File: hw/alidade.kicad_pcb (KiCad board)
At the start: 2 copper layers, 277.2 x 107.5 mm, 194 parts, among them J1 TYPE-C-31-M-13C, M1 SK8701-01-005-SENSOR, SW1 SW_Push, SW10 SW_Push, SW11 SW_Push, SW12 SW_Push, SW13 SW_Push, SW14 SW_Push, SW15 SW_Push, SW16 SW_Push, SW17 SW_Push, SW18 SW_Push, SW19 SW_Push, SW2 SW_Push, SW20 SW_Push, SW21 SW_Push, SW3 SW_Push, SW4 SW_Push, SW5 SW_Push, SW6 SW_Push, SW7 SW_Push, SW8 SW_Push, SW9 SW_Push, U1 NPM1300-QEAA-R, U2 NRF54L15-QFAA-R, U3 ADS122S14IRTER, Y1 ABS07-32.768KHZ-T, Y2 ABM8G-32.000MHZ-B4Y-T

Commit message: Place ftdi parts
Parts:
- added C24: 47p, Alidade:C_0603_1608Metric, F.Cu at (199.6, 149.9)
- added C25: 47p, Alidade:C_0603_1608Metric, F.Cu at (191.8, 142.1)
- added C26: 100n, Alidade:C_0603_1608Metric, F.Cu at (198.1, 149.9)
- added C27: 4.7u, Alidade:C_0603_1608Metric, F.Cu at (193.0, 145.9)
- added C28: 100n, Alidade:C_0603_1608Metric, F.Cu at (193.0, 144.4)
- added R1: 27, Alidade:R_0603_1608Metric, F.Cu at (193.3, 142.1)
- added R26: 27, Alidade:R_0603_1608Metric, F.Cu at (199.5, 144.3)
- added U5: FT200XD, Alidade:DFN-10_FTD, F.Cu at (196.7, 146.1)
- added U6: USBLC6-2SC6, Alidade:SOT23-6L_STM, F.Cu at (196.7, 142.3)
- added rC24: 47p, Alidade:C_0603_1608Metric, F.Cu at (218.6, 143.1)
- added rC25: 47p, Alidade:C_0603_1608Metric, F.Cu at (211.1, 140.8)
- added rC26: 100n, Alidade:C_0603_1608Metric, F.Cu at (218.8, 146.6)
- added rC27: 4.7u, Alidade:C_0603_1608Metric, F.Cu at (211.1, 149.8)
- added rC28: 100n, Alidade:C_0603_1608Metric, F.Cu at (212.6, 149.8)
- added rR1: 27, Alidade:R_0603_1608Metric, F.Cu at (211.1, 144.1)
- added rR26: 27, Alidade:R_0603_1608Metric, F.Cu at (217.1, 143.1)
- added rU5: FT200XD, Alidade:DFN-10_FTD, F.Cu at (213.9, 146.1)
- added rU6: USBLC6-2SC6, Alidade:SOT23-6L_STM, F.Cu at (213.9, 142.4)
- L1, L2, rL1, rL2: value 2.2uH -> 2.2u
- turned C1 to 180 degrees
- turned rC1 to 180 degrees
- renumbered rU4 to rU2
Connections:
- C1 pad 1: Net-(U1C-VBUS) -> GND
- C1 pad 2: GND -> /PMIC/VBUS
- J1 pad A4: Net-(U1C-VBUS) -> /PMIC/VBUS
- J1 pad A6: unconnected-(J1-D+-PadA6) -> Net-(J1-D+-PadA6)
- J1 pad A7: unconnected-(J1-D--PadA7) -> Net-(J1-D--PadA7)
- J1 pad A9: Net-(U1C-VBUS) -> /PMIC/VBUS
- J1 pad B4: Net-(U1C-VBUS) -> /PMIC/VBUS
- J1 pad B6: unconnected-(J1-D+-PadB6) -> Net-(J1-D+-PadA6)
- J1 pad B7: unconnected-(J1-D--PadB7) -> Net-(J1-D--PadA7)
- J1 pad B9: Net-(U1C-VBUS) -> /PMIC/VBUS
- U1 pad 10: /MCU/PMICGPIO3 -> unconnected-(U1B-GPIO3-Pad10)
- U1 pad 21: Net-(U1C-VBUS) -> /PMIC/VBUS
- U1 pad 7: unconnected-(U1B-GPIO0-Pad7) -> /MCU/PMICINT
- U1 pad 8: /MCU/PMICINT -> /MCU/PMICGPIO1
- U1 pad 9: /MCU/PMICGPIO2 -> unconnected-(U1B-GPIO2-Pad9)
- U2 pad 23: /MCU/PMICGPIO2 -> /MCU/PMICINT
- U2 pad 24: /MCU/PMICGPIO3 -> /MCU/PMICGPIO1
- U2 pad 27: /MCU/PMICINT -> Net-(U2D-P0.02)
- U2 pad 3: unconnected-(U2B-P1.02/NFC1-Pad3) -> /MCU/CBUS0
- rC1 pad 1: Net-(rU1C-VBUS) -> rGND
- rC1 pad 2: rGND -> /PMIC/rVBUS
- rJ1 pad A4: Net-(rU1C-VBUS) -> /PMIC/rVBUS
- rJ1 pad A6: unconnected-(rJ1-D+-PadA6) -> Net-(rJ1-D+-PadA6)
- rJ1 pad A7: unconnected-(rJ1-D--PadA7) -> Net-(rJ1-D--PadA7)
- rJ1 pad A9: Net-(rU1C-VBUS) -> /PMIC/rVBUS
- rJ1 pad B4: Net-(rU1C-VBUS) -> /PMIC/rVBUS
- rJ1 pad B6: unconnected-(rJ1-D+-PadB6) -> Net-(rJ1-D+-PadA6)
- rJ1 pad B7: unconnected-(rJ1-D--PadB7) -> Net-(rJ1-D--PadA7)
- rJ1 pad B9: Net-(rU1C-VBUS) -> /PMIC/rVBUS
- rU1 pad 10: /MCU/rPMICGPIO3 -> unconnected-(rU1B-GPIO3-Pad10)
- rU1 pad 21: Net-(rU1C-VBUS) -> /PMIC/rVBUS
- rU1 pad 7: unconnected-(rU1B-GPIO0-Pad7) -> /MCU/rPMICINT
- rU1 pad 8: /MCU/rPMICINT -> /MCU/rPMICGPIO1
- rU1 pad 9: /MCU/rPMICGPIO2 -> unconnected-(rU1B-GPIO2-Pad9)
- rU2 pad 23: /MCU/rPMICGPIO2 -> /MCU/rPMICINT
- rU2 pad 24: /MCU/rPMICGPIO3 -> /MCU/rPMICGPIO1
- rU2 pad 27: /MCU/rPMICINT -> Net-(rU2D-P0.02)
- rU2 pad 3: unconnected-(rU4B-P1.02/NFC1-Pad3) -> /MCU/rCBUS0
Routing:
- net /PMIC/VBUS: track 0.00 -> 39.6 mm, vias 0 -> 3
- net /PMIC/rVBUS: track 0.00 -> 31.4 mm, vias 0 -> 2
- net Net-(U1C-VBUS): track 22.2 -> 0.00 mm, vias 2 -> 0
- net Net-(rU1C-VBUS): track 22.1 -> 0.00 mm, vias 2 -> 0
- net /MCU/SDA: track 0.00 -> 21.2 mm
- net /MCU/SCL: track 0.00 -> 17.9 mm
- net Net-(J1-D--PadA7): track 0.00 -> 8.67 mm, vias 0 -> 1
- net Net-(rJ1-D+-PadA6): track 0.00 -> 8.21 mm, vias 0 -> 2
- net Net-(rJ1-D--PadA7): track 0.00 -> 7.18 mm, vias 0 -> 1
- net Net-(J1-D+-PadA6): track 0.00 -> 6.85 mm, vias 0 -> 3
- net Net-(rR26-Pad1): track 0.00 -> 5.61 mm
- net Net-(rU5A-USBDM): track 0.00 -> 5.47 mm
- net Net-(U5A-USBDP): track 0.00 -> 5.26 mm
- net Net-(R1-Pad1): track 0.00 -> 5.12 mm
- net Net-(U5A-USBDM): track 0.00 -> 4.78 mm
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
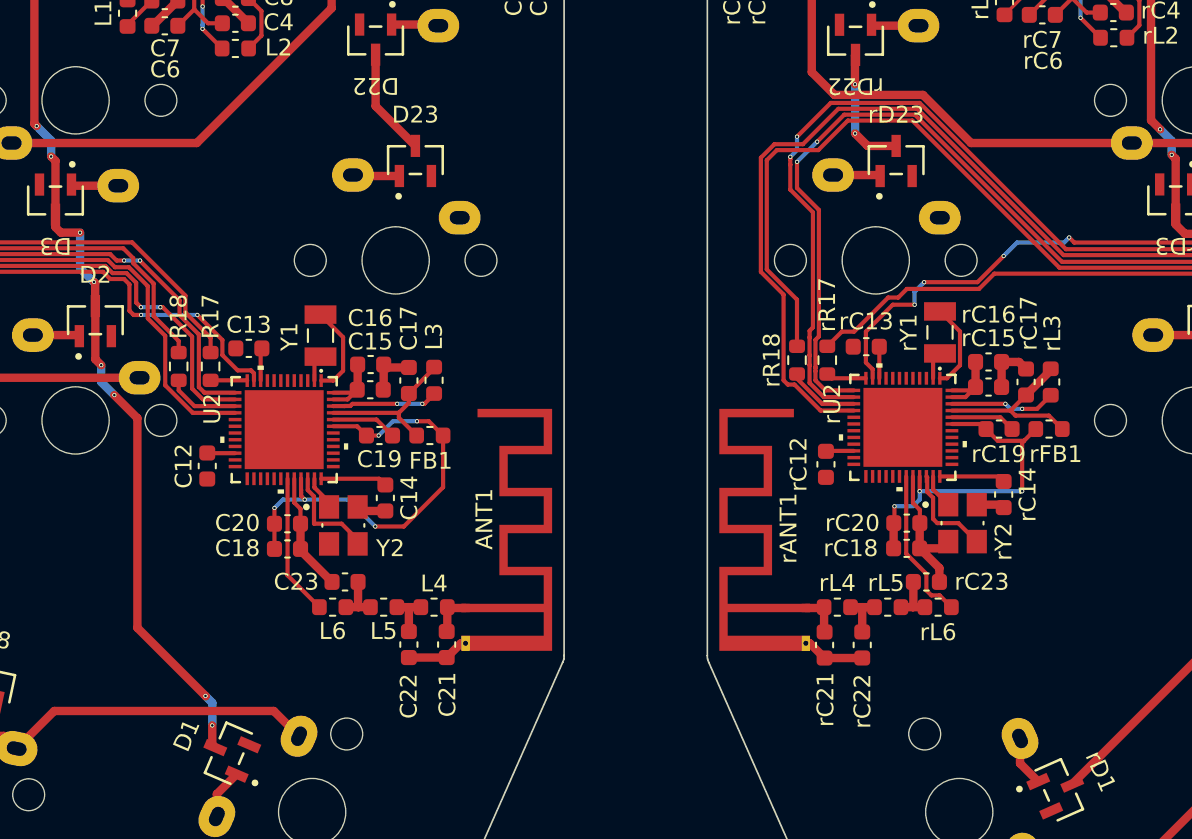
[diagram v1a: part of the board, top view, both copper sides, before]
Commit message: Remove mcu because it was wrong
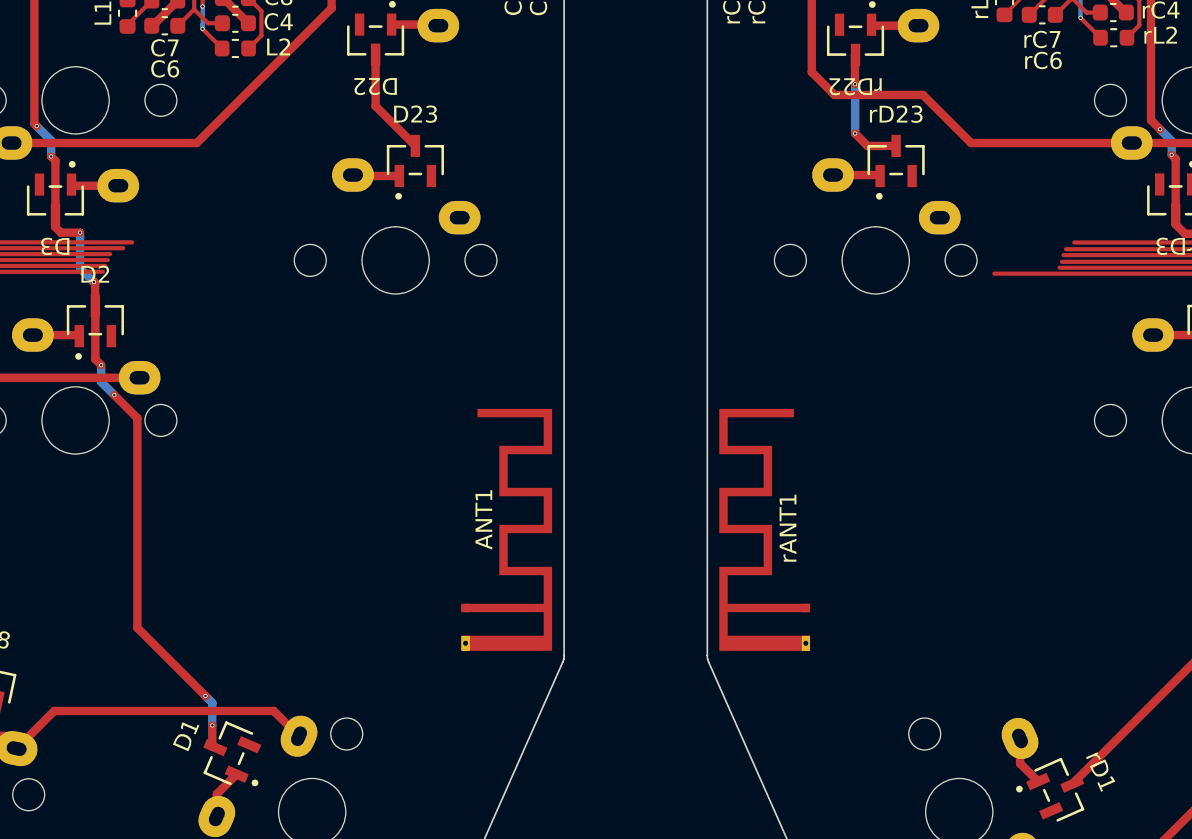
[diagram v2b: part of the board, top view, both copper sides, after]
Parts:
- removed C12, C13, C14, C15, rC12, rC13, rC14, rC15: 100n, Alidade:C_0603_1608Metric
- removed C16, rC16: 10u, Alidade:C_0603_1608Metric
- removed C17, C18, rC17, rC18: 2.2u, Alidade:C_0603_1608Metric
- removed C19, rC19: 10n, Alidade:C_0603_1608Metric
- removed C20, rC20: 2.2n, Alidade:C_0603_1608Metric
- removed C21, rC21: 0.3p, Alidade:C_0603_1608Metric
- removed C22, rC22: 2p, Alidade:C_0603_1608Metric
- removed C23, rC23: 1.5p, Alidade:C_0603_1608Metric
- removed FB1, rFB1: FB, Alidade:L_0603_1608Metric
- removed L3, rL3: 4.7u, Alidade:L_0603_1608Metric
- removed L4, L5, rL4, rL5: 3.5n, Alidade:L_0603_1608Metric
- removed L6, rL6: 2.7n, Alidade:L_0603_1608Metric
- removed R17, R18, rR17, rR18: 0, Alidade:R_0603_1608Metric
- removed U2, rU2: NRF54L15-QFAA-R, Alidade:QFN48_6X6
- removed Y1, rY1: ABS07-32.768KHZ-T, Alidade:XTAL_ABS07-32.768KHZ-1-T
- removed Y2, rY2: ABM8G-32.000MHZ-B4Y-T, Alidade:XTAL_ABM8G-32.000MHZ-B4Y-T
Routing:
- net /HID/rADCCS: track 92.9 -> 51.4 mm
- net /HID/rDRDY: track 89.0 -> 50.1 mm, vias 2 -> 0
- net /HID/rMISO: track 89.6 -> 52.9 mm, vias 2 -> 0
- net /HID/rMOSI: track 88.1 -> 54.3 mm
- net Net-(U2F-DECA): track 26.5 -> 0.00 mm, vias 5 -> 0
- net GND: track 54.8 -> 33.2 mm
- net rGND: track 53.5 -> 32.5 mm
- net Net-(rU2F-DECA): track 20.3 -> 0.00 mm, vias 3 -> 0
- net /HID/rFAULT: track 67.3 -> 49.1 mm, vias 4 -> 0
- net /HID/ADCCS: track 61.3 -> 47.1 mm
- net /HID/DRDY: track 62.4 -> 48.8 mm, vias 2 -> 0
- net /HID/FAULT: track 64.2 -> 50.9 mm, vias 2 -> 0
- net /HID/MISO: track 59.2 -> 46.0 mm, vias 2 -> 0
- net DVDD: track 22.5 -> 10.2 mm
- net rDVDD: track 21.4 -> 9.32 mm
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
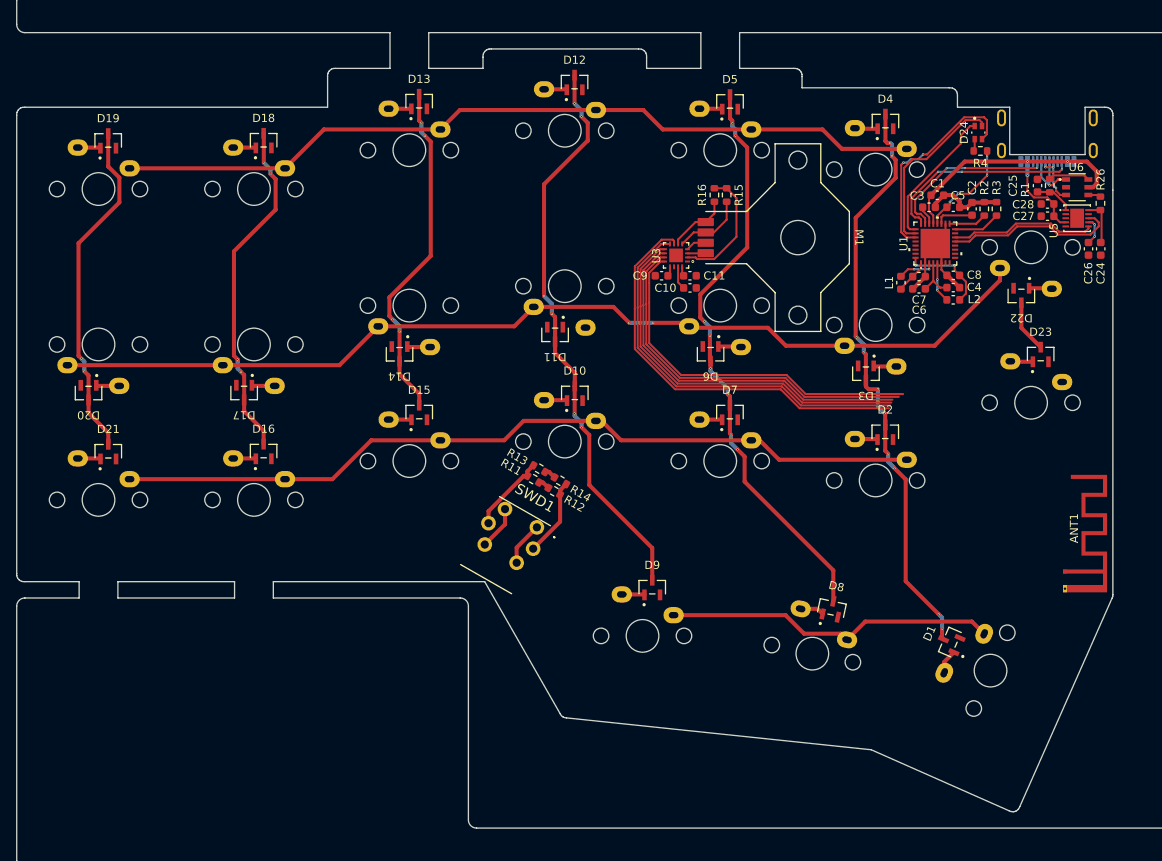
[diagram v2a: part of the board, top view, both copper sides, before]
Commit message: Add ground fills and attach left side
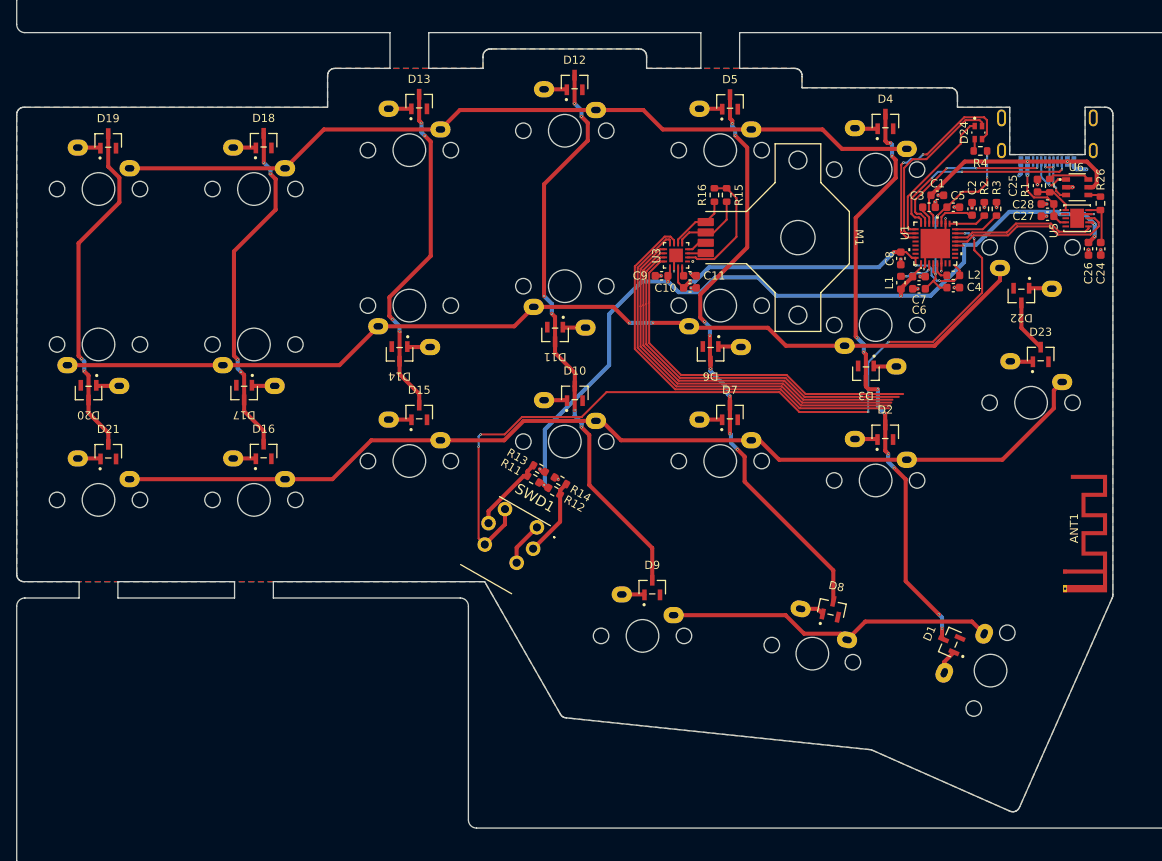
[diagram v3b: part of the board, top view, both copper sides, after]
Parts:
- moved C8 6.76 mm to (175.1, 151.0), turned to -90 degrees
- moved L2 3.00 mm to (181.5, 153.1)
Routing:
- net DVDD: track 10.2 -> 108.0 mm, vias 2 -> 7
- net /HID/SHPHLD: track 5.37 -> 103.2 mm, vias 0 -> 6
- net AVDD: track 13.7 -> 42.8 mm, vias 2 -> 4
- net /HID/ROW3: track 100.2 -> 124.5 mm
- net /PMIC/VSYS: track 17.6 -> 25.4 mm
- net GND: track 33.2 -> 39.2 mm, vias 0 -> 28
- net Net-(D11-A): track 0.00 -> 2.80 mm
- net Net-(U1F-SW2): track 4.96 -> 2.44 mm, vias 2 -> 0
- net /HID/DRDY: track 48.8 -> 49.6 mm
- added copper zone on B.Cu, net GND
- added copper zone on F.Cu, net GND
- added copper zone on In1.Cu, net GND
- added copper zone on In2.Cu, net GND
- added copper zone on In1.Cu, net rGND
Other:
- copper layers 2 -> 4

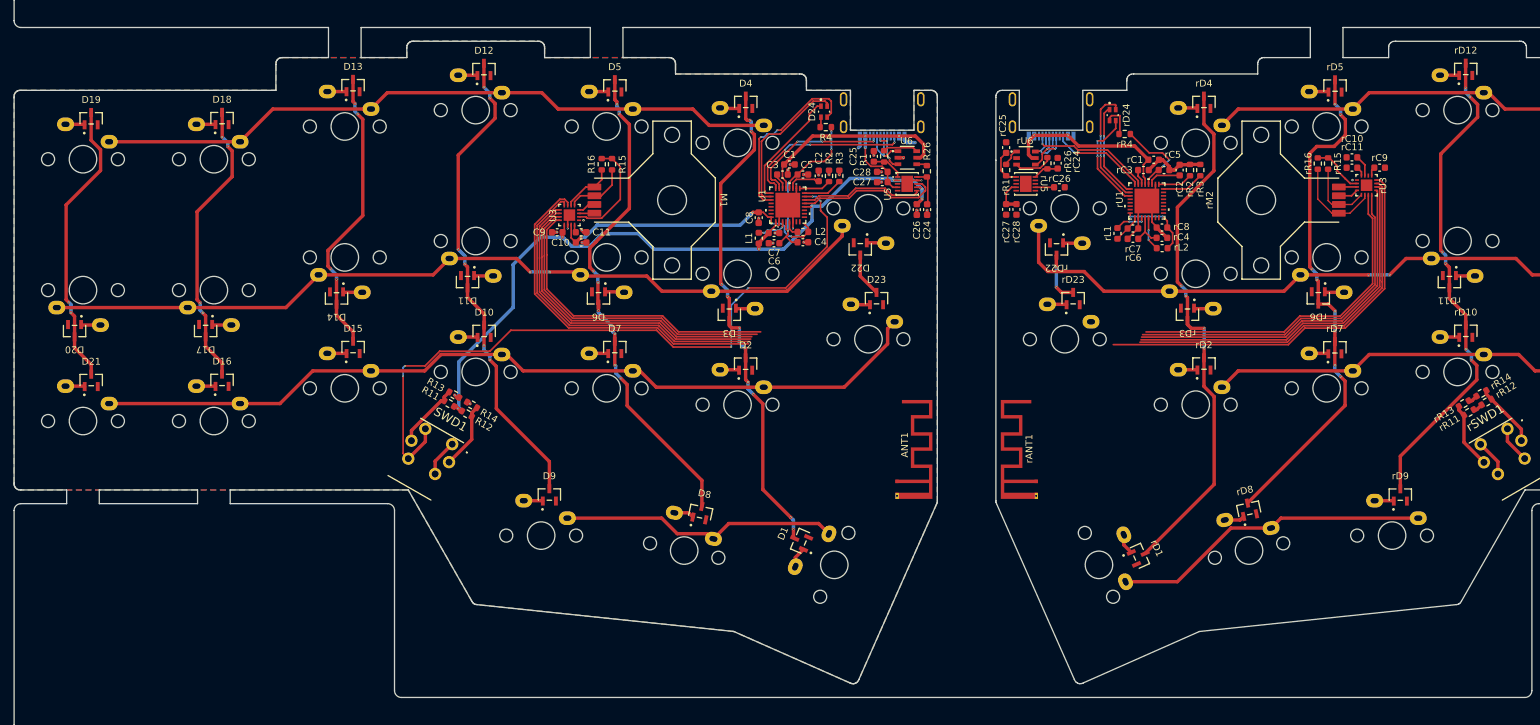
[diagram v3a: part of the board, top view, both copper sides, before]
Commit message: Ground plane for right side
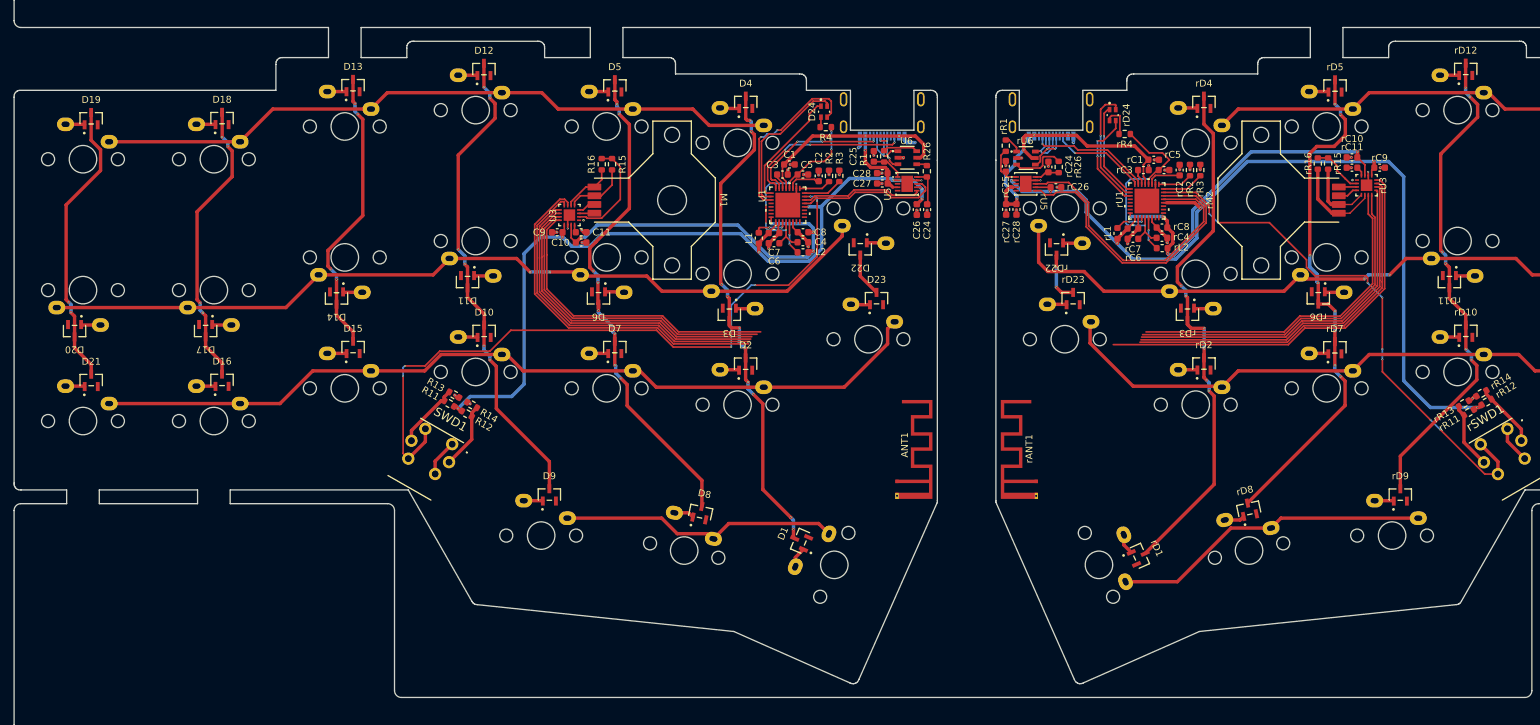
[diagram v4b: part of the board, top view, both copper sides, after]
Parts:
- moved C8 6.78 mm to (181.5, 153.2), turned to 180 degrees
- moved rR1 3.55 mm to (211.0, 140.6)
- moved L2 2.96 mm to (181.5, 156.1)
- moved rC25 2.73 mm to (211.0, 143.6)
- moved rR26 1.74 mm to (218.7, 143.7)
- moved rC24 1.46 mm to (217.2, 143.7)
- moved rC26 0.50 mm to (218.3, 146.6)
- moved C27 0.20 mm to (193.0, 146.1)
- moved C28 0.20 mm to (193.0, 144.6)
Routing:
- net rDVDD: track 9.32 -> 131.6 mm, vias 0 -> 6
- net /HID/rSHPHLD: track 5.36 -> 79.1 mm, vias 0 -> 8
- net /MCU/rSCL: track 0.00 -> 43.2 mm
- net /MCU/rSDA: track 0.00 -> 42.1 mm
- net rAVDD: track 14.1 -> 51.8 mm, vias 2 -> 4
- net /HID/rROW3: track 100.2 -> 125.2 mm
- net /PMIC/rVSYS: track 17.7 -> 30.0 mm
- net /PMIC/rVBUS: track 31.4 -> 43.3 mm, vias 2 -> 4
- net AVDD: track 42.8 -> 53.0 mm
- net DVDD: track 108.0 -> 117.2 mm
- net /PMIC/VSYS: track 25.4 -> 30.7 mm, vias 4 -> 6
- net Net-(U1F-SW2): track 2.44 -> 4.92 mm, vias 0 -> 2
- net Net-(rR26-Pad1): track 5.61 -> 7.99 mm
- net GND: track 39.2 -> 41.3 mm, vias 28 -> 24
- net rGND: track 32.5 -> 34.5 mm, vias 0 -> 23
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- added copper zone on In2.Cu, net rGND
- removed copper zone on B.Cu, net GND
- removed copper zone on F.Cu, net GND

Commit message: Place eeprom
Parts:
- added R25: 10k, Alidade:R_0603_1608Metric, F.Cu at (198.9, 174.9)
- added R5: 10k, Alidade:R_0603_1608Metric, F.Cu at (196.7, 161.4)
- added R6: 10k, Alidade:R_0603_1608Metric, F.Cu at (198.2, 162.2)
- added U4: AT24C32E-STUM-T, Alidade:TSOT5_MC_MCH, F.Cu at (198.3, 172.3)
- added rR25: 10k, Alidade:R_0603_1608Metric, F.Cu at (211.8, 174.9)
- added rR5: 10k, Alidade:R_0603_1608Metric, F.Cu at (211.9, 164.5)
- added rR6: 10k, Alidade:R_0603_1608Metric, F.Cu at (213.4, 165.5)
- added rU4: AT24C32E-STUM-T, Alidade:TSOT5_MC_MCH, F.Cu at (212.3, 172.3)
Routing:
- net rDVDD: track 131.6 -> 166.8 mm, vias 6 -> 10
- net DVDD: track 117.2 -> 151.5 mm, vias 7 -> 11
- net /MCU/rSCL: track 43.2 -> 72.7 mm, vias 0 -> 2
- net /MCU/SDA: track 21.0 -> 49.1 mm
- net /MCU/SCL: track 17.7 -> 45.2 mm, vias 0 -> 2
- net /MCU/rSDA: track 42.1 -> 69.2 mm, vias 0 -> 4
- net Net-(U2D-P0.02): track 0.00 -> 4.12 mm
- net Net-(rU2D-P0.02): track 0.00 -> 1.61 mm
- net /HID/ROW3: track 124.5 -> 125.2 mm
- net /HID/rADCCS: track 51.4 -> 52.1 mm
- net rGND: track 34.5 -> 35.2 mm, vias 23 -> 24
- net GND: track 41.3 -> 41.9 mm, vias 24 -> 25
- net /HID/rMISO: track 52.9 -> 53.4 mm
- net /HID/rMOSI: track 54.3 -> 54.8 mm
